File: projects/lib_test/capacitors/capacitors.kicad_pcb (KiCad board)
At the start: 2 copper layers, 80 x 40 mm, 77 parts

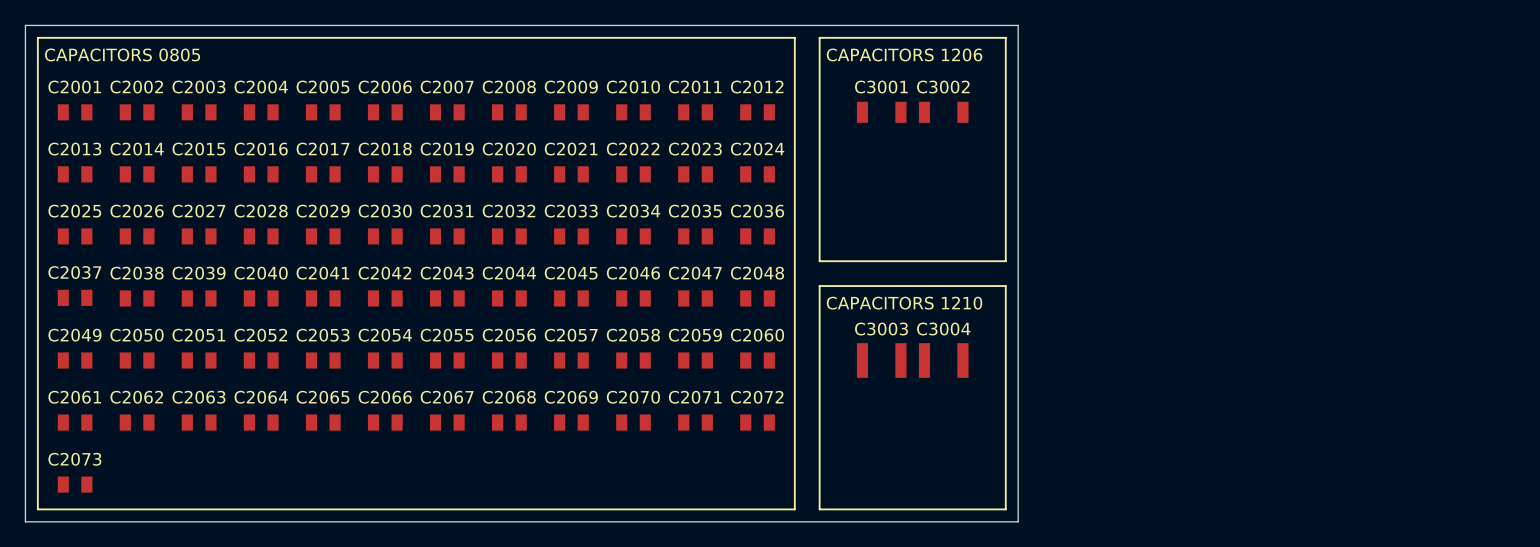
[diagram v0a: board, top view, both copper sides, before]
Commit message: change board outline
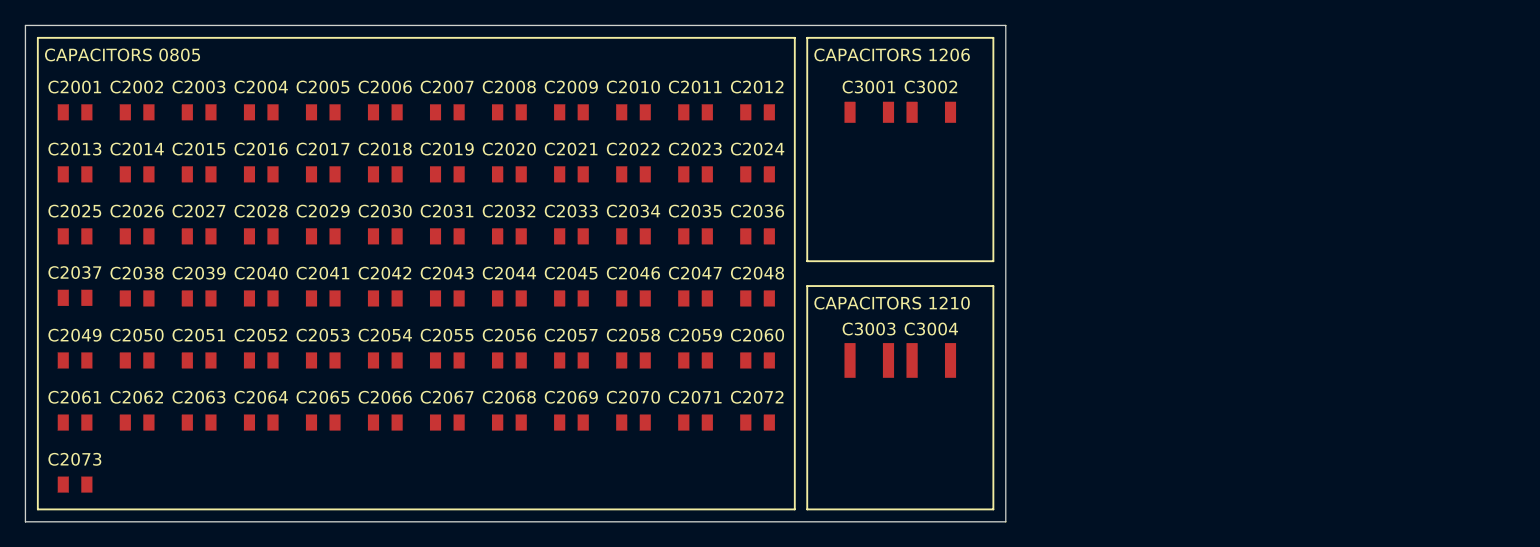
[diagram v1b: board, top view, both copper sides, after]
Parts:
- moved C3001 1.00 mm to (169.0, 55.0)
- moved C3002 1.00 mm to (174.0, 55.0)
- moved C3003 1.00 mm to (169.0, 75.0)
- moved C3004 1.00 mm to (174.0, 75.0)
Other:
- board size 80 x 40 mm -> 79 x 40 mm
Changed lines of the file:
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@@
 			(psa4output no)
 			(plot_black_and_white yes)
-			(plotinvisibletext no)
 			(sketchpadsonfab no)
 			(plotpadnumbers no)
@@
 	(footprint "lily_footprints:cap_1210_dnp"
 		(layer "F.Cu")
-		(at 175 75)
+		(at 174 75)
 		(property "Reference" "C3004"
 			(at 0 -2.5 0)
@@
 	(footprint "lily_footprints:cap_1206_dnp"
 		(layer "F.Cu")
-		(at 175 55)
+		(at 174 55)
 		(property "Reference" "C3002"
 			(at 0 -2 0)
@@
 	(footprint "lily_footprints:cap_1210"
 		(layer "F.Cu")
-		(at 170 75)
+		(at 169 75)
 		(property "Reference" "C3003"
 			(at 0 -2.5 0)
@@
 	(footprint "lily_footprints:cap_1206"
 		(layer "F.Cu")
-		(at 170 55)
+		(at 169 55)
 		(property "Reference" "C3001"
 			(at 0 -2 0)
@@
 	)
 	(gr_rect
-		(start 165 49)
-		(end 180 67)
+		(start 164 49)
+		(end 179 67)
 		(stroke
 			(width 0.15)
@@
 	)
 	(gr_rect
-		(start 165 69)
-		(end 180 87)
+		(start 164 69)
+		(end 179 87)
 		(stroke
 			(width 0.15)
@@
 	(gr_rect
 		(start 101 48)
-		(end 181 88)
+		(end 180 88)
 		(stroke
 			(width 0.1)
@@
 	)
 	(gr_text "CAPACITORS 1206"
-		(at 165.5 51 0)
+		(at 164.5 51 0)
 		(layer "F.SilkS")
 		(effects
@@
 	)
 	(gr_text "CAPACITORS 1210"
-		(at 165.5 71 0)
+		(at 164.5 71 0)
 		(layer "F.SilkS")
 		(effects

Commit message: add caps to test project
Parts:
- added C3005: 20p, lily_footprints:cap_trimmer_jz_series, F.Cu at (168.0, 55.0)
- moved C3001 10.2 mm to (167.0, 65.0)
- moved C3002 10.2 mm to (172.0, 65.0)
- moved C3003 4.47 mm to (167.0, 79.0)
- moved C3004 4.47 mm to (172.0, 79.0)
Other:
- board size 79 x 40 mm -> 82 x 40 mm
- board text added: "CAPACITORS VARIABLE"

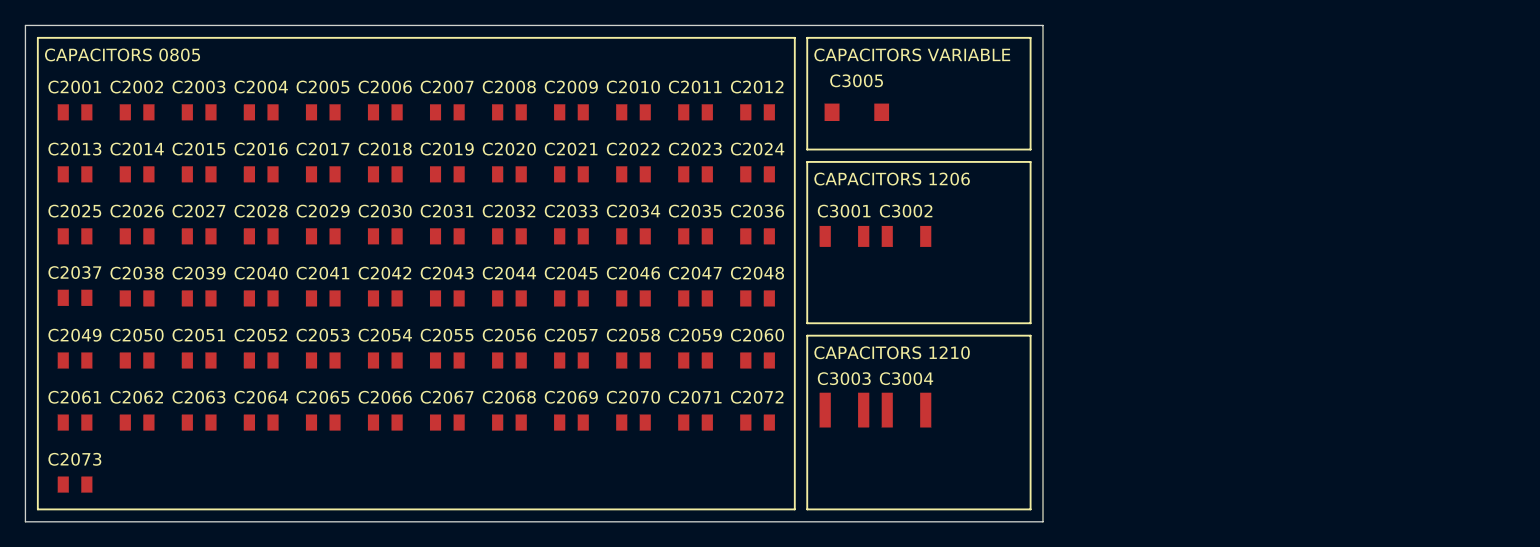
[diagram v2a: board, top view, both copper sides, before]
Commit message: updated capacitors test design
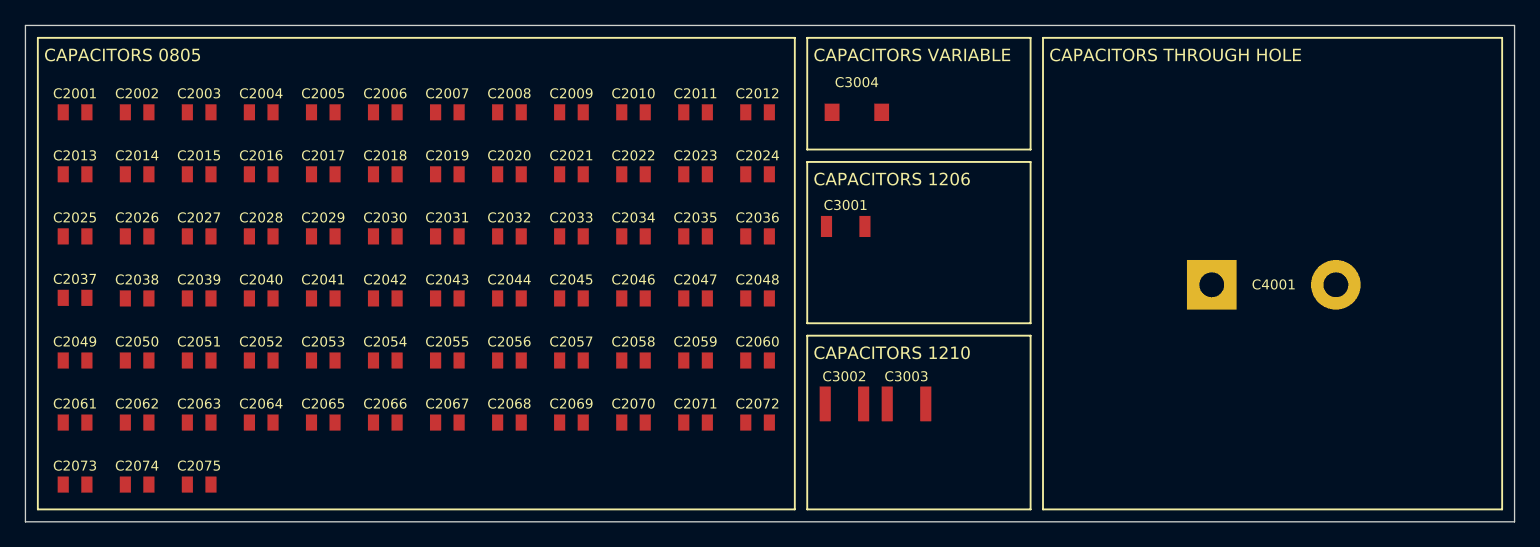
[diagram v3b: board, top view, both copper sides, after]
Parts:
- removed the C3001 at (167.0, 65.0)
- removed the C3003 at (167.0, 79.0)
- added C2074: 10u, lily_footprints:cap_0805, F.Cu at (110.0, 85.0)
- added C2075: 22u, lily_footprints:cap_0805, F.Cu at (115.0, 85.0)
- added C3002: 47u, lily_footprints:cap_1210, F.Cu at (167.0, 78.5)
- added C4001: 15m, lily_footprints:cap_elec_rad_35x52mm_th, F.Cu at (196.6, 68.9)
- moved C3001 4.96 mm to (167.1, 64.2)
- moved C3003 0.50 mm to (172.0, 78.5)
- renumbered C3002 to C3001, C3004 to C3003, C3005 to C3004
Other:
- board size 82 x 40 mm -> 120 x 40 mm
- board text added: "CAPACITORS THROUGH HOLE"
